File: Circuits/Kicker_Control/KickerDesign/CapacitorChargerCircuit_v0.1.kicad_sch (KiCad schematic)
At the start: 19 parts, among them Q2 NMOS, Q3 NMOS, T2 DA2034-ALD

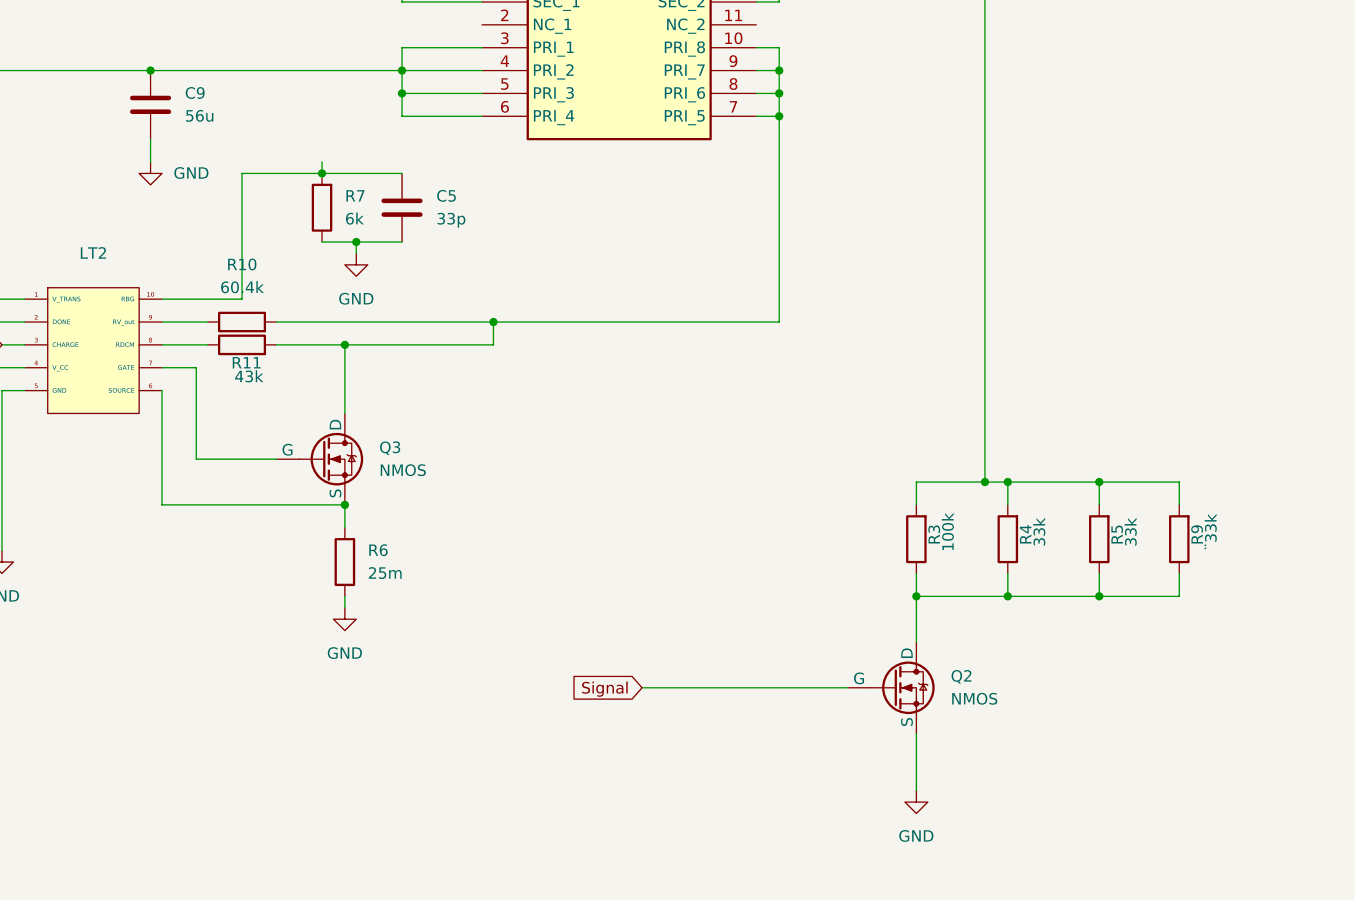
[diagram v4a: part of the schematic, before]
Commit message: Added components to the BOM and updated the capacitor circuit
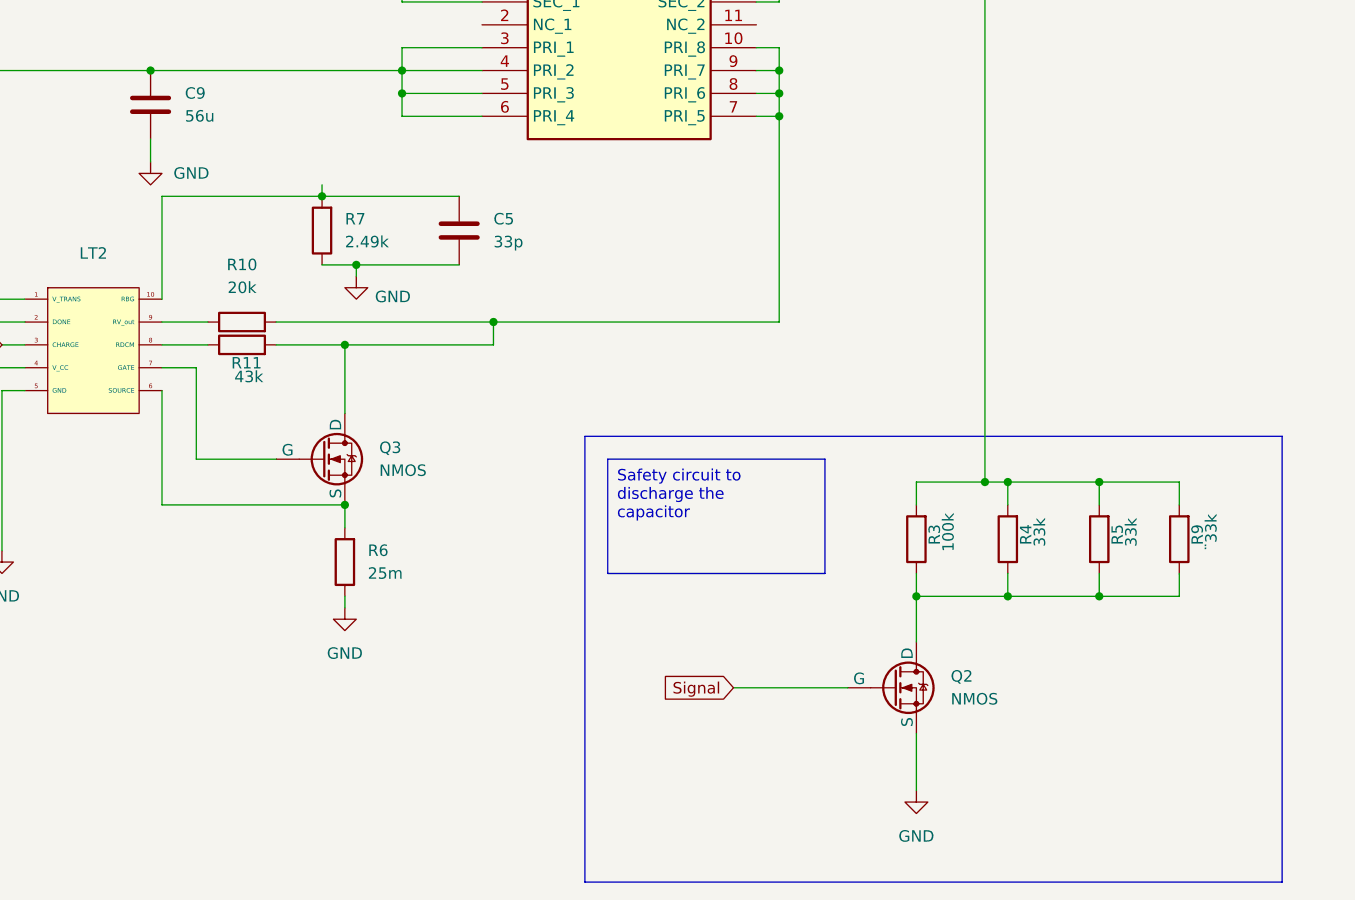
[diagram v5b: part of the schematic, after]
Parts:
- R10: value 60.4k -> 20k
- R7: value 6k -> 2.49k
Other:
- moved on the sheet: C5, R7
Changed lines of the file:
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@@
 	)
 	(junction
-		(at 173.99 81.28)
+		(at 173.99 83.82)
 		(diameter 0)
 		(color 0 0 0 0)
 	)
 	(junction
-		(at 170.18 73.66)
+		(at 170.18 76.2)
 		(diameter 0)
 		(color 0 0 0 0)
@@
 	(wire
 		(pts
-			(xy 170.18 73.66) (xy 179.07 73.66)
+			(xy 170.18 76.2) (xy 185.42 76.2)
 		)
 		(stroke
@@
 	(wire
 		(pts
-			(xy 161.29 87.63) (xy 161.29 73.66)
-		)
-		(stroke
-			(width 0)
-			(type default)
-		)
-	)
-	(wire
-		(pts
 			(xy 220.98 67.31) (xy 220.98 90.17)
 		)
@@
 	(wire
 		(pts
-			(xy 152.4 87.63) (xy 161.29 87.63)
+			(xy 152.4 76.2) (xy 170.18 76.2)
 		)
 		(stroke
@@
 	(wire
 		(pts
+			(xy 152.4 76.2) (xy 152.4 87.63)
+		)
+		(stroke
+			(width 0)
+			(type default)
+		)
+	)
+	(wire
+		(pts
 			(xy 256.54 110.49) (xy 256.54 107.95)
 		)
@@
 	(wire
 		(pts
-			(xy 173.99 81.28) (xy 179.07 81.28)
+			(xy 173.99 83.82) (xy 185.42 83.82)
 		)
 		(stroke
@@
 	(wire
 		(pts
-			(xy 170.18 81.28) (xy 173.99 81.28)
+			(xy 170.18 83.82) (xy 173.99 83.82)
 		)
 		(stroke
@@
 	(wire
 		(pts
-			(xy 170.18 72.39) (xy 170.18 73.66)
+			(xy 170.18 74.93) (xy 170.18 76.2)
 		)
 		(stroke
@@
 	(wire
 		(pts
-			(xy 173.99 81.28) (xy 173.99 82.55)
+			(xy 173.99 83.82) (xy 173.99 85.09)
 		)
 		(stroke
@@
 	(wire
 		(pts
-			(xy 161.29 73.66) (xy 170.18 73.66)
-		)
-		(stroke
-			(width 0)
-			(type default)
-		)
-	)
-	(wire
-		(pts
 			(xy 246.38 120.65) (xy 256.54 120.65)
 		)
@@
 	(wire
 		(pts
-			(xy 205.74 130.81) (xy 228.6 130.81)
+			(xy 215.9 130.81) (xy 228.6 130.81)
 		)
 		(stroke
@@
 			(width 0)
 			(type default)
+		)
+	)
+	(rectangle
+		(start 199.39 102.87)
+		(end 276.86 152.4)
+		(stroke
+			(width 0)
+			(type default)
+		)
+		(fill
+			(type none)
 		)
 	)
@@
 		)
 	)
+	(text_box "Safety circuit to discharge the capacitor"
+		(exclude_from_sim no)
+		(at 201.93 105.41 0)
+		(size 24.13 12.7)
+		(stroke
+			(width 0)
+			(type default)
+		)
+		(fill
+			(type none)
+		)
+		(effects
+			(font
+				(size 1.27 1.27)
+			)
+			(justify left top)
+		)
+	)
 	(global_label "Signal"
 		(shape input)
-		(at 205.74 130.81 180)
+		(at 215.9 130.81 180)
 		(fields_autoplaced yes)
 		(effects
@@
 		)
 		(property "Intersheetrefs" "${INTERSHEET_REFS}"
-			(at 196.8283 130.81 0)
+			(at 206.9883 130.81 0)
 			(effects
 				(font
@@
 	(symbol
 		(lib_id "Device:C")
-		(at 179.07 77.47 0)
+		(at 185.42 80.01 0)
 		(unit 1)
 		(exclude_from_sim no)
@@
 		(fields_autoplaced yes)
 		(property "Reference" "C5"
-			(at 182.88 76.1999 0)
+			(at 189.23 78.7399 0)
 			(effects
 				(font
@@
 		)
 		(property "Value" "33p"
-			(at 182.88 78.7399 0)
+			(at 189.23 81.2799 0)
 			(effects
 				(font
@@
 		)
 		(property "Footprint" ""
-			(at 180.0352 81.28 0)
+			(at 186.3852 83.82 0)
 			(effects
 				(font
@@
 		)
 		(property "Datasheet" "~"
-			(at 179.07 77.47 0)
+			(at 185.42 80.01 0)
 			(effects
 				(font
@@
 		)
 		(property "Description" "Unpolarized capacitor"
-			(at 179.07 77.47 0)
+			(at 185.42 80.01 0)
 			(effects
 				(font
@@
 	(symbol
 		(lib_id "power:GND")
-		(at 173.99 82.55 0)
+		(at 173.99 85.09 0)
 		(unit 1)
 		(exclude_from_sim no)
@@
 		(on_board yes)
 		(dnp no)
-		(fields_autoplaced yes)
 		(property "Reference" "#PWR05"
-			(at 173.99 88.9 0)
+			(at 173.99 91.44 0)
 			(effects
 				(font
@@
 		)
 		(property "Value" "GND"
-			(at 173.99 87.63 0)
+			(at 178.054 87.376 0)
 			(effects
 				(font
@@
 		)
 		(property "Footprint" ""
-			(at 173.99 82.55 0)
+			(at 173.99 85.09 0)
 			(effects
 				(font
@@
 		)
 		(property "Datasheet" ""
-			(at 173.99 82.55 0)
+			(at 173.99 85.09 0)
 			(effects
 				(font
@@
 		)
 		(property "Description" "Power symbol creates a global label with name \"GND\" , ground"
-			(at 173.99 82.55 0)
+			(at 173.99 85.09 0)
 			(effects
 				(font
@@
 	(symbol
 		(lib_id "Device:R")
-		(at 170.18 77.47 180)
+		(at 170.18 80.01 180)
 		(unit 1)
 		(exclude_from_sim no)
@@
 		(fields_autoplaced yes)
 		(property "Reference" "R7"
-			(at 172.72 76.1999 0)
+			(at 172.72 78.7399 0)
 			(effects
 				(font
@@
 			)
 		)
-		(property "Value" "6k"
-			(at 172.72 78.7399 0)
+		(property "Value" "2.49k"
+			(at 172.72 81.2799 0)
 			(effects
 				(font
@@
 		)
 		(property "Footprint" ""
-			(at 171.958 77.47 90)
+			(at 171.958 80.01 90)
 			(effects
 				(font
@@
 		)
 		(property "Datasheet" "~"
-			(at 170.18 77.47 0)
+			(at 170.18 80.01 0)
 			(effects
 				(font
@@
 		)
 		(property "Description" "Resistor"
-			(at 170.18 77.47 0)
+			(at 170.18 80.01 0)
 			(effects
 				(font
@@
 			)
 		)
-		(property "Value" "60.4k"
+		(property "Value" "20k"
 			(at 161.29 86.36 90)
 			(effects
